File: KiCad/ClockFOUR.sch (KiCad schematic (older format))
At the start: 40 parts, among them P1 ICSP, P2 FTDI, P3 LDR_header, P4 Button_Header, P5 BARREL_JACK, SW1 SW_RST, U1 ATMEGA328P, U2 DS3231N, X1 CRYSTAL

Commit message: Layout changes
+ increased size of 5V traces
+ board notch around RTC battery
+ added breakout pins
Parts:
- added S5, S6, S7, S8, S9: CONN_1, symbol CONN_1
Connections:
- net labels added: D3, D4, D5, D6, D7
- wire segments 228 -> 233
- no-connect marks 17 -> 12
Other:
- note added: "Breakout pins"
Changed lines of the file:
@@
 Sheet 1 14
 Title "ClockFOUR"
-Date "6 oct 2014"
+Date "7 oct 2014"
 Rev ""
 Comp "WyoLum"
@@
 C1 ED 35 72 E0 F7 FB FF F1 1F FF F1 9F FF F9 9F C7 C7 C7 73 1A 9F 2B 70 38 1C FB F6 ED 3B 79 F2
 E4 23 8F 3C 52 B0 F1 D9 2E 76 F1 FF 03 17 ED 19 47 28 92 59 FB 00 00 00 00 49 45 4E 44 AE 42 60
-82 02 $EndBitmap
+82 00 $EndBitmap
 EndData
 $EndBitmap
@@
 $EndSheet
 $Comp
-L GND #PWR9
+L GND #PWR01
 U 1 1 50E7FAEA
 P 5350 7125
-F 0 "#PWR9" H 5350 7125 30  0001 C CNN
+F 0 "#PWR01" H 5350 7125 30  0001 C CNN
 F 1 "GND" H 5350 7055 30  0001 C CNN
 F 2 "" H 5350 7125 60  0001 C CNN
@@
 $EndComp
 $Comp
-L GND #PWR6
+L GND #PWR02
 U 1 1 542A3CA4
 P 2850 4275
-F 0 "#PWR6" H 2850 4275 30  0001 C CNN
+F 0 "#PWR02" H 2850 4275 30  0001 C CNN
 F 1 "GND" H 2850 4205 30  0001 C CNN
 F 2 "" H 2850 4275 60  0000 C CNN
@@
 $EndComp
 $Comp
-L VCC #PWR7
+L VCC #PWR03
 U 1 1 542B825F
 P 2375 5350
-F 0 "#PWR7" H 2375 5450 30  0001 C CNN
+F 0 "#PWR03" H 2375 5450 30  0001 C CNN
 F 1 "VCC" H 2375 5450 30  0000 C CNN
 F 2 "" H 2375 5350 60  0000 C CNN
@@
 SCL
 $Comp
-L GND #PWR10
+L GND #PWR04
 U 1 1 542BA28D
 P 2625 7300
-F 0 "#PWR10" H 2625 7300 30  0001 C CNN
+F 0 "#PWR04" H 2625 7300 30  0001 C CNN
 F 1 "GND" H 2625 7230 30  0001 C CNN
 F 2 "" H 2625 7300 60  0000 C CNN
@@
 $EndComp
 $Comp
-L VCC #PWR2
+L VCC #PWR05
 U 1 1 542A1F5B
 P 5175 1250
-F 0 "#PWR2" H 5175 1350 30  0001 C CNN
+F 0 "#PWR05" H 5175 1350 30  0001 C CNN
 F 1 "VCC" H 5175 1350 30  0000 C CNN
 F 2 "" H 5175 1250 60  0000 C CNN
@@
 $EndComp
 $Comp
-L GND #PWR4
+L GND #PWR06
 U 1 1 542A20C7
 P 5175 2450
-F 0 "#PWR4" H 5175 2450 30  0001 C CNN
+F 0 "#PWR06" H 5175 2450 30  0001 C CNN
 F 1 "GND" H 5175 2380 30  0001 C CNN
 F 2 "" H 5175 2450 60  0000 C CNN
@@
 $EndComp
 $Comp
-L GND #PWR3
+L GND #PWR07
 U 1 1 542A5508
 P 6050 1550
-F 0 "#PWR3" H 6050 1550 30  0001 C CNN
+F 0 "#PWR07" H 6050 1550 30  0001 C CNN
 F 1 "GND" H 6050 1480 30  0001 C CNN
 F 2 "" H 6050 1550 60  0000 C CNN
@@
 $EndComp
 $Comp
-L GND #PWR5
+L GND #PWR08
 U 1 1 542A550E
 P 6050 2525
-F 0 "#PWR5" H 6050 2525 30  0001 C CNN
+F 0 "#PWR08" H 6050 2525 30  0001 C CNN
 F 1 "GND" H 6050 2455 30  0001 C CNN
 F 2 "" H 6050 2525 60  0000 C CNN
@@
 RESET
 NoConn ~ 4025 1575
-NoConn ~ 4025 3475
-NoConn ~ 4025 3575
-NoConn ~ 4025 3675
-NoConn ~ 4025 3775
-NoConn ~ 4025 3875
 NoConn ~ 4025 2875
 NoConn ~ 4025 2975
@@
 NoConn ~ 4025 1675
 $Comp
-L PWR_FLAG #FLG1
+L PWR_FLAG #FLG09
 U 1 1 542A828E
 P 950 5450
-F 0 "#FLG1" H 950 5720 30  0001 C CNN
+F 0 "#FLG09" H 950 5720 30  0001 C CNN
 F 1 "PWR_FLAG" H 950 5680 30  0000 C CNN
 F 2 "" H 950 5450 60  0000 C CNN
@@
 $EndComp
 $Comp
-L VCC #PWR1
+L VCC #PWR010
 U 1 1 542AE434
 P 2800 975
-F 0 "#PWR1" H 2800 1075 30  0001 C CNN
+F 0 "#PWR010" H 2800 1075 30  0001 C CNN
 F 1 "VCC" H 2800 1075 30  0000 C CNN
 F 2 "" H 2800 975 60  0000 C CNN
@@
 VCC
 $Comp
-L PWR_FLAG #FLG2
+L PWR_FLAG #FLG011
 U 1 1 542C2187
 P 5100 6350
-F 0 "#FLG2" H 5100 6445 30  0001 C CNN
+F 0 "#FLG011" H 5100 6445 30  0001 C CNN
 F 1 "PWR_FLAG" H 5100 6530 30  0000 C CNN
 F 2 "" H 5100 6350 60  0000 C CNN
@@
 $EndComp
 $Comp
-L PWR_FLAG #FLG3
+L PWR_FLAG #FLG012
 U 1 1 542C219E
 P 5350 7050
-F 0 "#FLG3" H 5350 7145 30  0001 C CNN
+F 0 "#FLG012" H 5350 7145 30  0001 C CNN
 F 1 "PWR_FLAG" H 5350 7230 30  0000 C CNN
 F 2 "" H 5350 7050 60  0000 C CNN
@@
 $EndComp
 $Comp
-L VCC #PWR8
+L VCC #PWR013
 U 1 1 542BE803
 P 6525 6500
-F 0 "#PWR8" H 6525 6600 30  0001 C CNN
+F 0 "#PWR013" H 6525 6600 30  0001 C CNN
 F 1 "VCC" H 6525 6600 30  0000 C CNN
 F 2 "" H 6525 6500 60  0000 C CNN
@@
 	4875 850  4875 3875
 Wire Notes Line
-	5700 850  5700 5000
+	5700 850  5700 5775
 Wire Wire Line
 	3800 2375 4025 2375
@@
 	6150 7000 6150 7050
 Connection ~ 6150 7050
+Text Label 4025 3475 0    60   ~ 0
+D3
+Text Label 4025 3575 0    60   ~ 0
+D4
+$Comp
+L CONN_1 S5
+U 1 1 5433999D
+P 6425 5125
+F 0 "S5" H 6505 5125 40  0000 L CNN
+F 1 "CONN_1" H 6425 5180 30  0001 C CNN
+F 2 "" H 6425 5125 60  0000 C CNN
+F 3 "" H 6425 5125 60  0000 C CNN
+	1    6425 5125
+	1    0    0    -1
+$EndComp
+$Comp
+L CONN_1 S6
+U 1 1 543399A3
+P 6425 5250
+F 0 "S6" H 6505 5250 40  0000 L CNN
+F 1 "CONN_1" H 6425 5305 30  0001 C CNN
+F 2 "" H 6425 5250 60  0000 C CNN
+F 3 "" H 6425 5250 60  0000 C CNN
+	1    6425 5250
+	1    0    0    -1
+$EndComp
+$Comp
+L CONN_1 S7
+U 1 1 543399A9
+P 6425 5375
+F 0 "S7" H 6505 5375 40  0000 L CNN
+F 1 "CONN_1" H 6425 5430 30  0001 C CNN
+F 2 "" H 6425 5375 60  0000 C CNN
+F 3 "" H 6425 5375 60  0000 C CNN
+	1    6425 5375
+	1    0    0    -1
+$EndComp
+$Comp
+L CONN_1 S8
+U 1 1 543399AF
+P 6425 5500
+F 0 "S8" H 6505 5500 40  0000 L CNN
+F 1 "CONN_1" H 6425 5555 30  0001 C CNN
+F 2 "" H 6425 5500 60  0000 C CNN
+F 3 "" H 6425 5500 60  0000 C CNN
+	1    6425 5500
+	1    0    0    -1
+$EndComp
+Wire Wire Line
+	6000 5125 6275 5125
+Wire Wire Line
+	6275 5250 6000 5250
+Wire Wire Line
+	6275 5375 6000 5375
+Wire Wire Line
+	6275 5500 6000 5500
+Text Label 6000 5125 0    60   ~ 0
+D3
+Text Label 6000 5250 0    60   ~ 0
+D4
+Text Label 4025 3675 0    60   ~ 0
+D5
+Text Label 4025 3775 0    60   ~ 0
+D6
+Text Label 4025 3875 0    60   ~ 0
+D7
+$Comp
+L CONN_1 S9
+U 1 1 5433A96F
+P 6425 5625
+F 0 "S9" H 6505 5625 40  0000 L CNN
+F 1 "CONN_1" H 6425 5680 30  0001 C CNN
+F 2 "" H 6425 5625 60  0000 C CNN
+F 3 "" H 6425 5625 60  0000 C CNN
+	1    6425 5625
+	1    0    0    -1
+$EndComp
+Text Label 6000 5375 0    60   ~ 0
+D5
+Text Label 6000 5500 0    60   ~ 0
+D6
+Text Label 6000 5625 0    60   ~ 0
+D7
+Text Notes 5750 5750 0    60   ~ 0
+Breakout pins
+Wire Notes Line
+	5700 5775 6675 5775
+Wire Wire Line
+	6275 5625 6000 5625
 $EndSCHEMATC

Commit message: Anool's version of pcb saved as ClockFOUR_anool.kicad_pcb
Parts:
- removed BT1: BATT_RTC, ~, symbol BATT_RTC
- added BT1: Batt_RTC, symbol Batt_RTC
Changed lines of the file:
@@
 LIBS:ClockFOUR
 LIBS:ClockFOUR-cache
-EELAYER 27 0
+EELAYER 24 0
 EELAYER END
 $Descr A4 11693 8268
@@
 C1 ED 35 72 E0 F7 FB FF F1 1F FF F1 9F FF F9 9F C7 C7 C7 73 1A 9F 2B 70 38 1C FB F6 ED 3B 79 F2
 E4 23 8F 3C 52 B0 F1 D9 2E 76 F1 FF 03 17 ED 19 47 28 92 59 FB 00 00 00 00 49 45 4E 44 AE 42 60
-82 00 $EndBitmap
+82 DC
 EndData
 $EndBitmap
@@
 NoConn ~ 5900 4575
 $Comp
-L BATT_RTC BT1
-U 1 1 542CF9F1
-P 950 6325
-F 0 "BT1" H 900 6125 50  0000 C CNN
-F 1 "BATT_RTC" H 900 6200 50  0000 C CNN
-F 2 "~" H 950 6325 60  0000 C CNN
-F 3 "~" H 950 6325 60  0000 C CNN
-F 4 "BU2032SM-HD-GCT-ND " H 1050 6625 60  0001 C CNN "Digikey"
-	1    950  6325
-	0    1    1    0
-$EndComp
-$Comp
 L ATMEGA328P U1
 U 1 1 542D5902
@@
 Wire Wire Line
 	6275 5625 6000 5625
+$Comp
+L Batt_RTC BT1
+U 1 1 54356384
+P 950 6325
+F 0 "BT1" H 1150 6225 50  0000 C CNN
+F 1 "Batt_RTC" H 1050 6150 50  0000 C CNN
+F 2 "" H 950 6325 60  0000 C CNN
+F 3 "" H 950 6325 60  0000 C CNN
+F 4 "BU2032SM-HD-GCT-ND " H 1050 6625 60  0001 C CNN "Digikey"
+	1    950  6325
+	0    1    1    0
+$EndComp
 $EndSCHEMATC

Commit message: PCB layout, work in progress
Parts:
- removed X1: CRYSTAL, ~, symbol CRYSTAL
- added X1: 16MHz, symbol CRYSTAL_3
- BT1: footprint (none) -> C4_Pretty:CR2032
- C1, C11, C2, C3, C4, C5, C6, C7, C8, C9: footprint (none) -> C4_Pretty:c_0805
- C10, C194, C195, C196: footprint TinyTiM_Lib:c_2917 -> C4_Pretty:c_2917
- L1: footprint TinyTiM_Lib:OSHW_6mm -> C4_Pretty:Logo_silk_OSHW_6x6mm
- L2: footprint TinyTiM_Lib:Logo-WL3 -> C4_Pretty:Logo-WL3
- LDR1, R1, R2, R3, R4, R5, R6, R7, R8, R9: footprint ~ -> C4_Pretty:r_0805
- P1: footprint (none) -> C4_Pretty:ISP
- P2: footprint (none) -> C4_Pretty:Header_FTDI
- P3, P4: footprint (none) -> C4_Pretty:SIL-2
- P5: footprint (none) -> C4_Pretty:JACK_PJ-047a
- S1, S2, S3, S4: footprint (none) -> C4_Pretty:Screw_3mm
- S5, S6, S7, S8, S9: footprint (none) -> C4_Pretty:BreakOutPad
- SW1: footprint ~ -> C4_Pretty:SW_PB_V_H
- U1: footprint TQFP32 -> C4_Pretty:TQFP32
- U2: footprint ~ -> C4_Pretty:DS3231
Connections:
- wire segments 233 -> 234
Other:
- moved on the sheet: C4, C6

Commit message: C4 PCB layout complete. Added Gerbers
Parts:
- added C197, C198: 100n, C4_Pretty:c_0805, symbol CAP_NP
- added P6: 5VEN_L, C4_Pretty:r_0805, symbol CONN_2
- added P7: I2C_L, C4_Pretty:STACK-L, symbol CONN_4
- added P8: 5VEN_R, C4_Pretty:r_0805, symbol CONN_2
- added P9: I2C_R, C4_Pretty:STACK-R, symbol CONN_4
- added S10, S11, S12, S13: CONN_1, C4_Pretty:Screw_2mm, symbol CONN_1
- BT1: footprint C4_Pretty:CR2032 -> C4_Pretty:CR2032_SMD
- X1: footprint (none) -> C4_Pretty:Xtal_SMD3
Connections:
- net GND: now also C197.2, C198.2, P7.4, P9.1
- net SCL: now also P7.2, P9.3
- net SDA: now also P7.3, P9.2
- net VCC: now also P6.1 (P1), P8.1 (P1)
- new net 5V_L: C197.1, P6.2 (PM), P7.1
- new net 5V_R: C198.1, P8.2 (PM), P9.4
- no-connect marks 12 -> 16
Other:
- note added: "I2C Connectors"
- note added: "Power Cord\nAncorage Holes"
- moved on the sheet: BT1, C1, C10, C11, C194, C195, C196, C2, C3, C4, C5, C6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

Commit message: C4 PCB layout complete. BoM in progress
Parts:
- BT1: footprint C4_Pretty:CR2032_SMD -> C4_Pretty:CR2032_SMD2
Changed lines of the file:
@@
 C1 ED 35 72 E0 F7 FB FF F1 1F FF F1 9F FF F9 9F C7 C7 C7 73 1A 9F 2B 70 38 1C FB F6 ED 3B 79 F2
 E4 23 8F 3C 52 B0 F1 D9 2E 76 F1 FF 03 17 ED 19 47 28 92 59 FB 00 00 00 00 49 45 4E 44 AE 42 60
-82 B7
+82 87
 EndData
 $EndBitmap
@@
 F 0 "BT1" V 850 5950 40  0000 C CNN
 F 1 "Batt_RTC" H 1100 5950 40  0000 C CNN
-F 2 "C4_Pretty:CR2032_SMD" H 950 6025 60  0001 C CNN
+F 2 "C4_Pretty:CR2032_SMD2" H 950 6025 60  0001 C CNN
 F 3 "" H 950 6025 60  0000 C CNN
 F 4 "BU2032SM-HD-GCT-ND " H 1050 6325 60  0001 C CNN "Digikey"

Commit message: C4 board layout complete. Gerbers and BoM ready
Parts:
- R1: value 500R -> 470R
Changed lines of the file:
@@
 EESchema Schematic File Version 2
 LIBS:ClockFOUR
-LIBS:RowGB_sym
 LIBS:ClockFOUR-cache
-EELAYER 24 0
+EELAYER 25 0
 EELAYER END
 $Descr A4 11693 8268
@@
 C1 ED 35 72 E0 F7 FB FF F1 1F FF F1 9F FF F9 9F C7 C7 C7 73 1A 9F 2B 70 38 1C FB F6 ED 3B 79 F2
 E4 23 8F 3C 52 B0 F1 D9 2E 76 F1 FF 03 17 ED 19 47 28 92 59 FB 00 00 00 00 49 45 4E 44 AE 42 60
-82 87
+82 97
 EndData
 $EndBitmap
@@
 P 8550 650
 F 0 "R1" V 8500 850 40  0000 C CNN
-F 1 "500R" V 8557 651 40  0000 C CNN
+F 1 "470R" V 8557 651 40  0000 C CNN
 F 2 "C4_Pretty:r_0805" V 8480 650 30  0001 C CNN
 F 3 "~" H 8550 650 30  0000 C CNN

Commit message: C4 added spare buttons, SMD push buttons, I2C address ports etc
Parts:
- added B2: CONN_1, C4_Pretty:BreakOutPad, symbol CONN_1
- added L3: Wyolum, C4_Pretty:Logo-WL3, symbol CONN_1
- added R10, R11: 10K, C4_Pretty:r_0805, symbol R
- added R12, R13: 0R, C4_Pretty:r_0805, symbol R
- added SW2: SW_L, C4_Pretty:SW_SMD, symbol SW_PUSH
- added SW3: SW_R, C4_Pretty:SW_SMD, symbol SW_PUSH
- P6, P8: symbol CONN_2 -> R
- SW1: footprint C4_Pretty:SW_PB_V_H -> C4_Pretty:SW_SMD
- renumbered S5 to A6, S6 to A7
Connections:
- net 5V_L: now also P6.1; no longer P6.2 (PM)
- net GND: now also R10.2, R11.2, R12.1, R13.1
- net VCC: now also P6.2, SW2.1, SW3.1; no longer P6.1 (P1)
- net BAT: now reaches BT1.1 (+), C9.1, U2.14 (Vbat)
- net at U1.12 ((PCINT0/CLKO/ICP1)PB0): now also R12.2
- net at U1.13 ((PCINT1/OC1A)PB1): now also R13.2
- net B2: now reaches U1.14 ((PCINT2/OC1B/~SS~)PB2)
- net B2: now also B2.1
- net A6: now reaches U1.19 (ADC6)
- net A6: now also A6.1
- net AREF: now reaches C3.1, U1.20 (AREF)
- net A7: now reaches U1.22 (ADC7)
- net A7: now also A7.1
- net D3 renamed SW_L
- net SW_L: now also R10.1, SW2.2; no longer A6.1
- net D4 renamed SW_R
- net SW_R: now also R11.1, SW3.2; no longer A7.1
- no-connect marks 16 -> 12
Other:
- note added: "Push Buttons"
- note added: "Solder Bridges for\nHW Addressing"
- moved on the sheet: A7, C1, C10, C11, C194, C195, C196, C3, C5, C7, L1, L2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

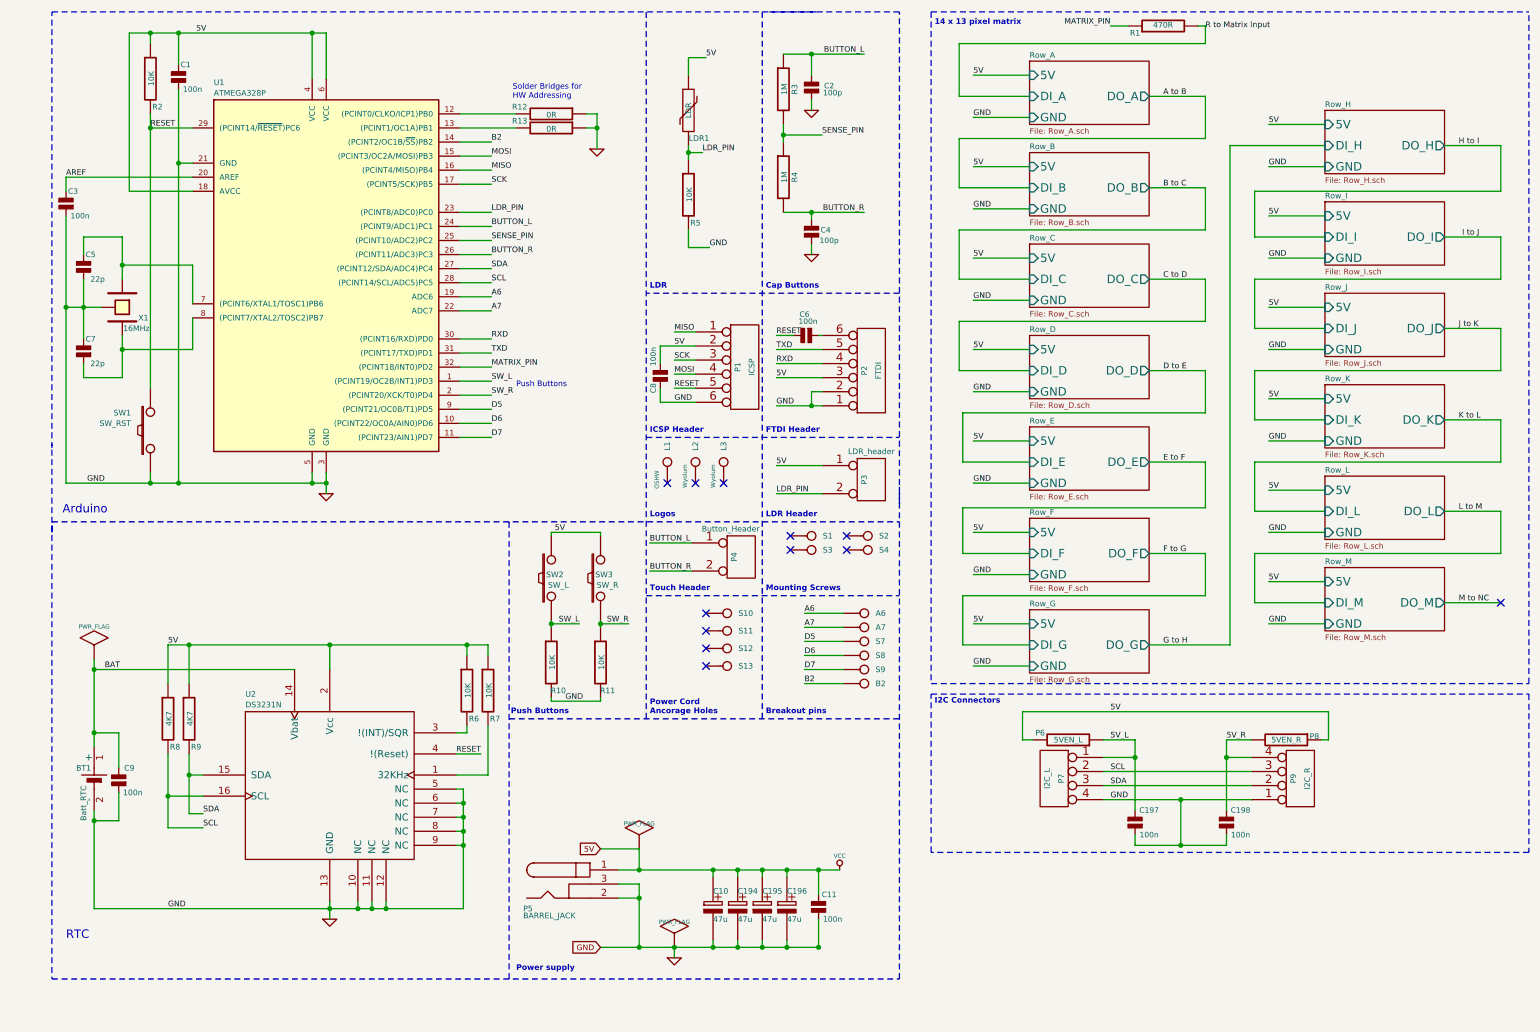
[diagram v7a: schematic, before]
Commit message: C4 added NiL header
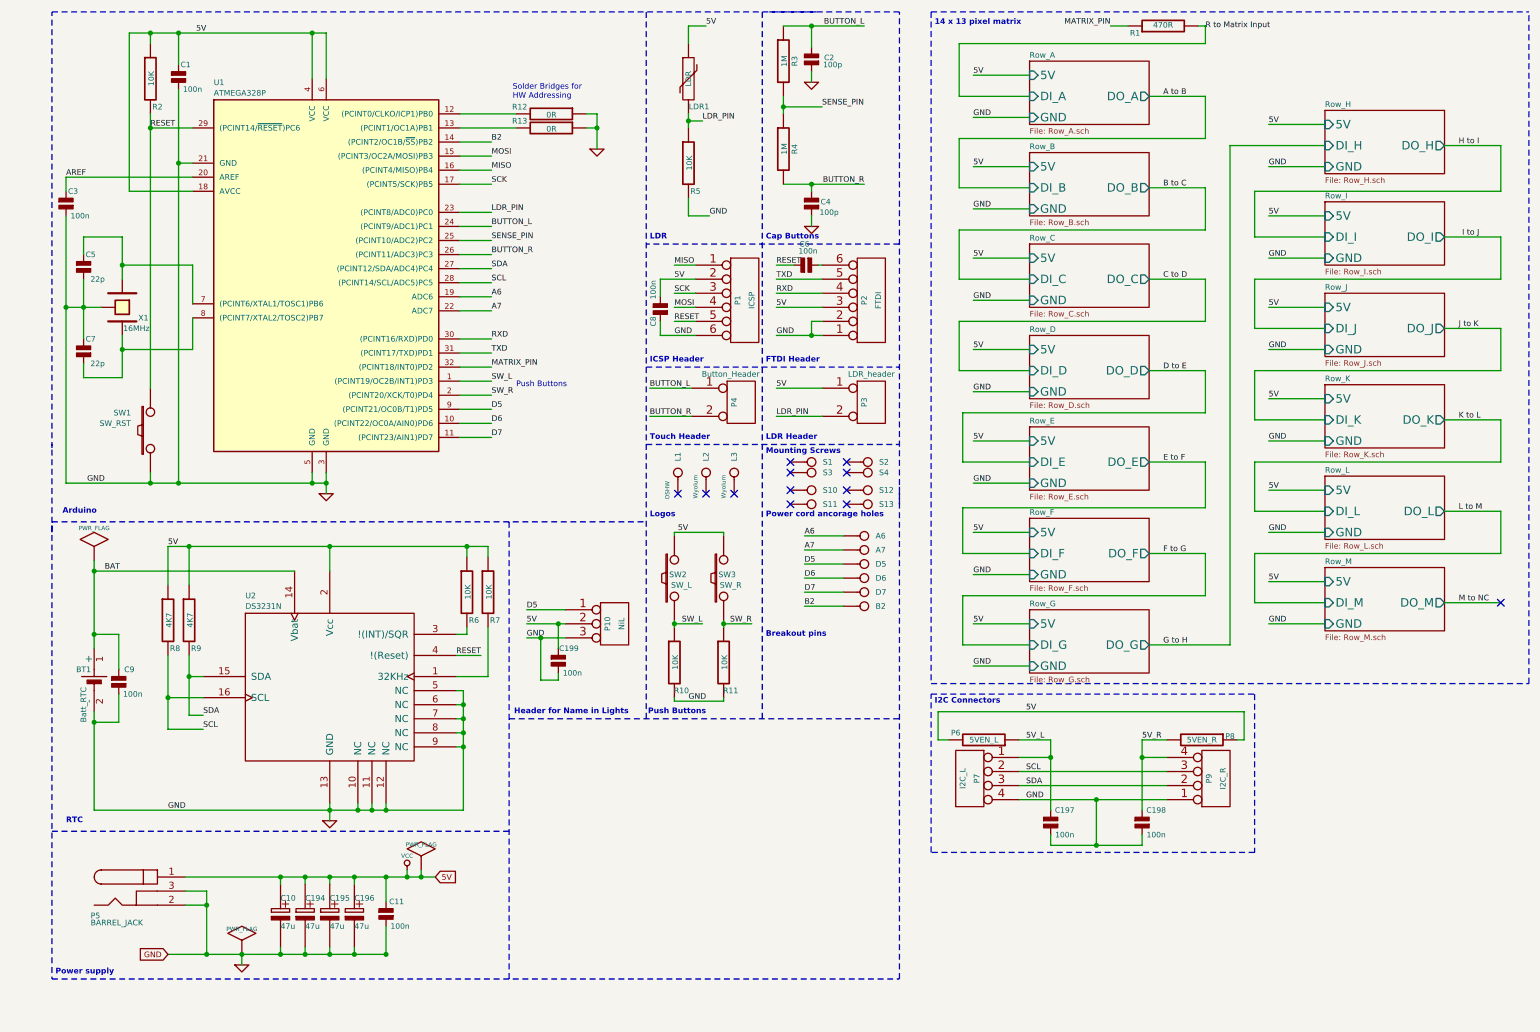
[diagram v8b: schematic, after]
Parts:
- added C199: 100n, C4_Pretty:c_0805, symbol CAP_NP
- added P10: NiL, C4_Pretty:Header_3x1, symbol CONN_3
- renumbered S7 to D5, S8 to D6, S9 to D7
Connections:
- net D5: now also P10.1
- net GND: now also C199.2, P10.3
- net VCC: now also C199.1, P10.2
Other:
- note added: "Header for Name in Lights"
- note added: "Power cord ancorage holes"
- note removed: "Power Cord\nAncorage Holes"
- moved on the sheet: A6, A7, B2, BT1, C10, C11, C194, C195, C196, C197, C198, C2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
